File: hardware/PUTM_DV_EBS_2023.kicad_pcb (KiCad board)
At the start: 4 copper layers, 100 x 70 mm, 158 parts, among them IC1 UCC2946DG4, IC2 SN74LVC1G74DCTR, IC3 SN74LVC1G74DCTR, J1 SAFETY_SUPPLY, J2 SWDIO_CONN, J3 SENSORS, J4 VALVES, J5 MAIN, K1 FINDER-30.22, K2 FINDER-30.22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

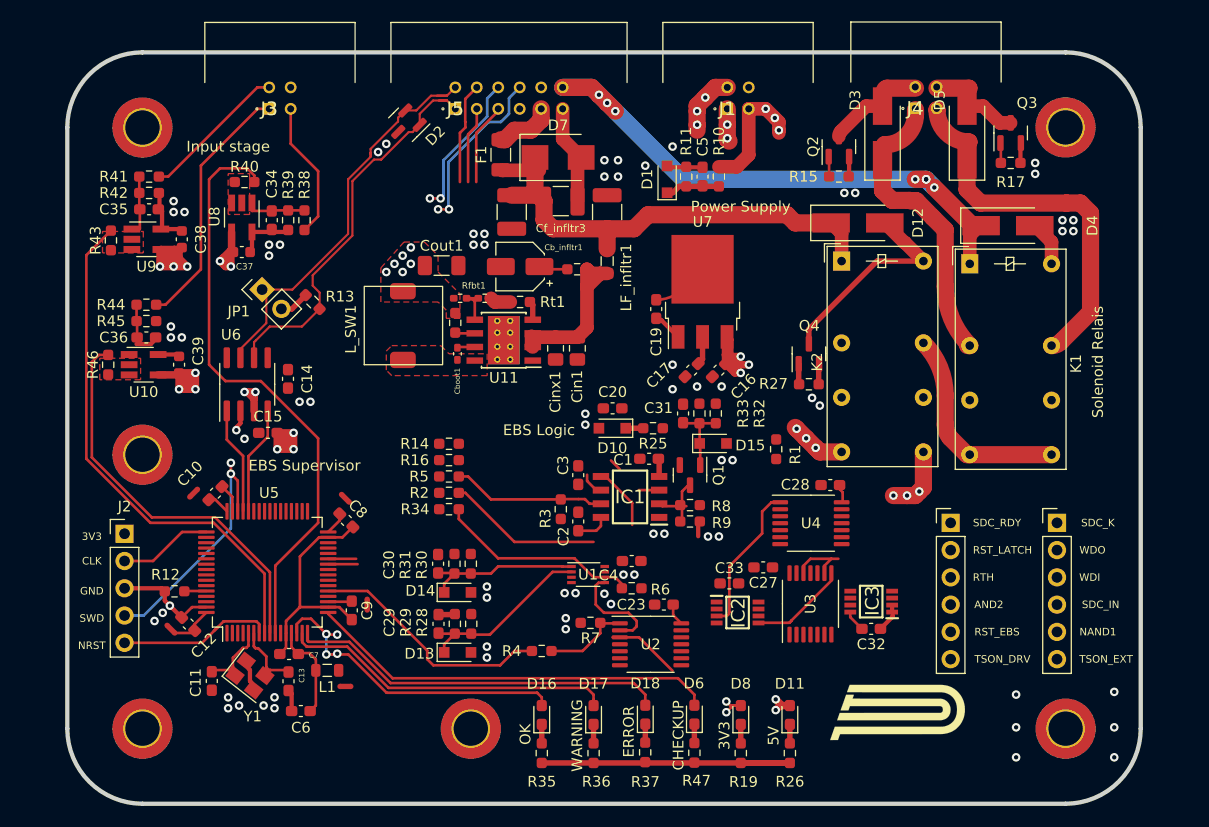
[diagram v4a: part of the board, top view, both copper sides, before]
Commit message: PCB in review and DRC error delete state, please check it
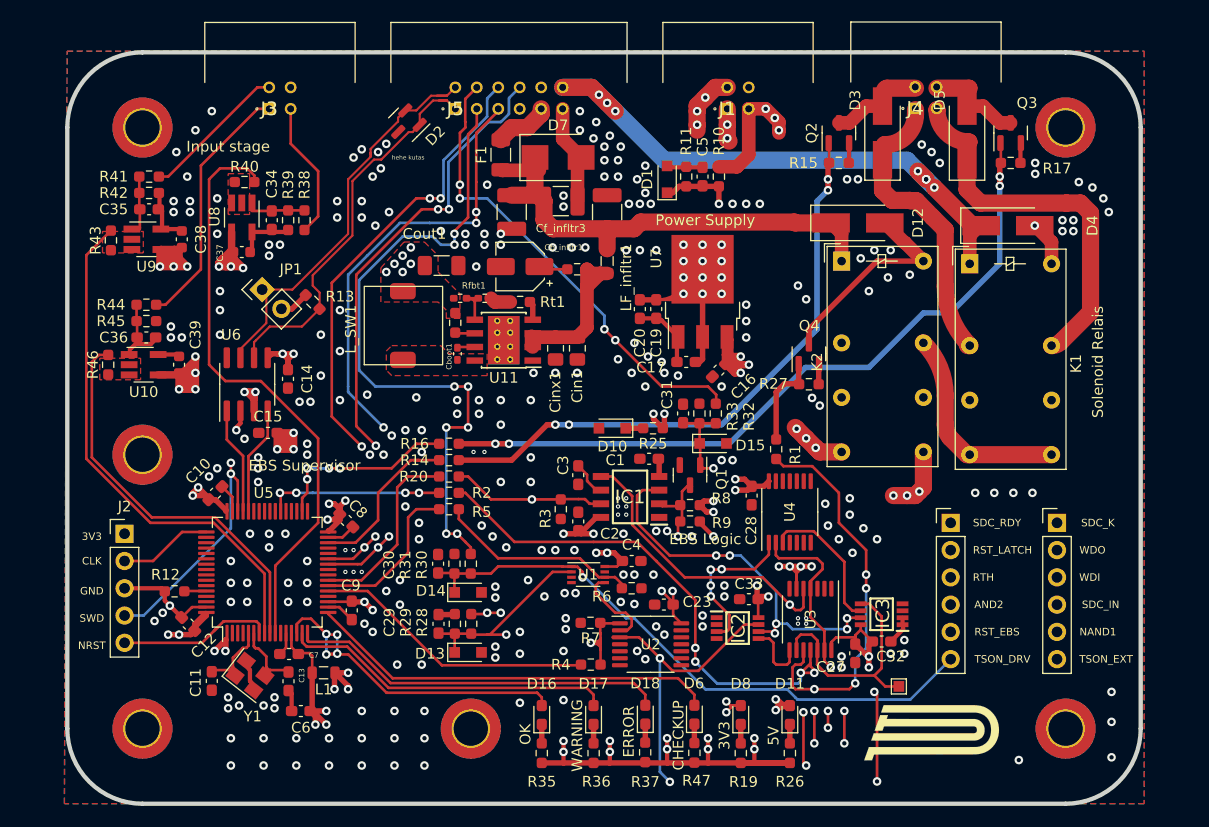
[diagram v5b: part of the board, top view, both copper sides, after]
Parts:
- removed NT1 (x5): NetTie_2, NetTie:NetTie-2_SMD_Pad0.5mm
- removed R34: 2.2k, Resistor_SMD:R_0603_1608Metric_Pad0.98x0.95mm_HandSolder
- added R20: 2.2k, Resistor_SMD:R_0603_1608Metric_Pad0.98x0.95mm_HandSolder, F.Cu at (128.5, 70.6)
- added REF**: TestPoint_Pad_1.0x1.0mm, TestPoint:TestPoint_Pad_1.0x1.0mm, F.Cu at (170.4, 90.2)
- moved G*** 60.8 mm to (131.6, 69.3)
- moved C27 11.7 mm to (166.4, 87.1), turned to -90 degrees
- moved C20 9.59 mm to (146.3, 55.0), turned to -90 degrees
- moved C28 7.39 mm to (156.7, 72.4), turned to -90 degrees
- moved R4 4.75 mm to (141.7, 88.1)
- moved G*** 3.70 mm to (173.1, 94.4)
- moved R5 3.05 mm to (128.5, 73.7)
- moved C33 2.34 mm to (156.5, 82.0)
- moved U4 2.23 mm to (160.3, 73.9), turned to 90 degrees
- moved C32 1.53 mm to (168.8, 86.0)
- moved IC3 1.53 mm to (168.8, 83.4)
- moved R14 1.52 mm to (128.5, 69.1)
- moved R16 1.52 mm to (128.5, 67.6)
- moved IC2 1.45 mm to (155.4, 84.7)
- moved U3 1.45 mm to (162.2, 83.9), turned to -90 degrees
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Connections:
- C10 pad 1: /EBS Supervisor/3V3_SYS -> +3V3
- C12 pad 1: /EBS Supervisor/3V3_SYS -> +3V3
- C8 pad 1: /EBS Supervisor/3V3_SYS -> +3V3
- C9 pad 1: /EBS Supervisor/3V3_SYS -> +3V3
- L1 pad 1: /EBS Supervisor/3V3_SYS -> +3V3
- R5 pad 2: /EBS Logic/WATCHDOG -> /EBS Logic/AS_DRIVING_MODE
- REF** pad 1: (no net) -> /EBS Logic/AS_CLOSE_SDC
- REF** pad 2: (no net) -> Net-(IC1-Pad5)
- REF** pad 3: (no net) -> /EBS Logic/WATCHDOG
- REF** pad 4: (no net) -> /EBS Logic/SAFETY_IN
- REF** pad 5: (no net) -> /EBS Logic/AS COMMANDS OK
- REF** pad 6: (no net) -> /EBS Logic/TS_ON_EXT
- REF** pad 1: (no net) -> /EBS Logic/SDC READY
- REF** pad 2: (no net) -> /EBS Logic/RESET BUTTON LATCH
- REF** pad 3: (no net) -> Net-(IC1-Pad2)
- REF** pad 4: (no net) -> /EBS Logic/WD + SAFETY OK
- REF** pad 5: (no net) -> /EBS Logic/SAFETY_RESET_BUT
- REF** pad 6: (no net) -> /EBS Logic/TS_ON_COCKPIT
- U5 pad 1: /EBS Supervisor/3V3_SYS -> +3V3
- U5 pad 19: /EBS Supervisor/3V3_SYS -> +3V3
- U5 pad 32: /EBS Supervisor/3V3_SYS -> +3V3
- U5 pad 48: /EBS Supervisor/3V3_SYS -> +3V3
- U5 pad 64: /EBS Supervisor/3V3_SYS -> +3V3
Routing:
- net /EBS Logic/SAFETY_IN: track 5.07 -> 107.8 mm, vias 0 -> 10
- net +3V3: track 29.1 -> 117.6 mm, vias 2 -> 49
- net /EBS Logic/WATCHDOG: track 14.4 -> 101.5 mm, vias 0 -> 1
- net /EBS Logic/SDC READY: track 14.4 -> 96.1 mm, vias 0 -> 6
- net /EBS Logic/RESET BUTTON LATCH: track 1.93 -> 80.4 mm, vias 0 -> 8
- net Net-(IC1-Pad5): track 5.97 -> 83.4 mm, vias 0 -> 3
- net /EBS Logic/TS_ON_EXT: track 17.4 -> 89.6 mm, vias 0 -> 1
- net /EBS Logic/AS_CLOSE_SDC: track 8.05 -> 80.1 mm, vias 0 -> 1
- net /EBS Logic/AS COMMANDS OK: track 6.89 -> 75.9 mm, vias 0 -> 2
- net Net-(Q3-Pad1): track 1.87 -> 68.7 mm, vias 0 -> 4
- net Net-(IC1-Pad2): track 6.43 -> 69.5 mm, vias 0 -> 1
- net /EBS Logic/SAFETY_RESET_BUT: track 6.99 -> 68.0 mm, vias 0 -> 1
- net TS_ON_EXTERNAL: track 7.67 -> 67.3 mm, vias 0 -> 6
- net DASH_TS_ON: track 7.15 -> 62.8 mm, vias 0 -> 8
- net Net-(Q2-Pad1): track 1.87 -> 56.3 mm, vias 0 -> 4
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- added copper zone on In1.Cu, net +3V3
- added copper zone on B.Cu, net GND
- added copper zone on F.Cu, net GND
- added copper zone on In2.Cu, net GND
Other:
- board text added: "hehe kutas"
